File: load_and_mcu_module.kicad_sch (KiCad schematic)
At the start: 1 part, among them M2 LP-MSPM0G3519

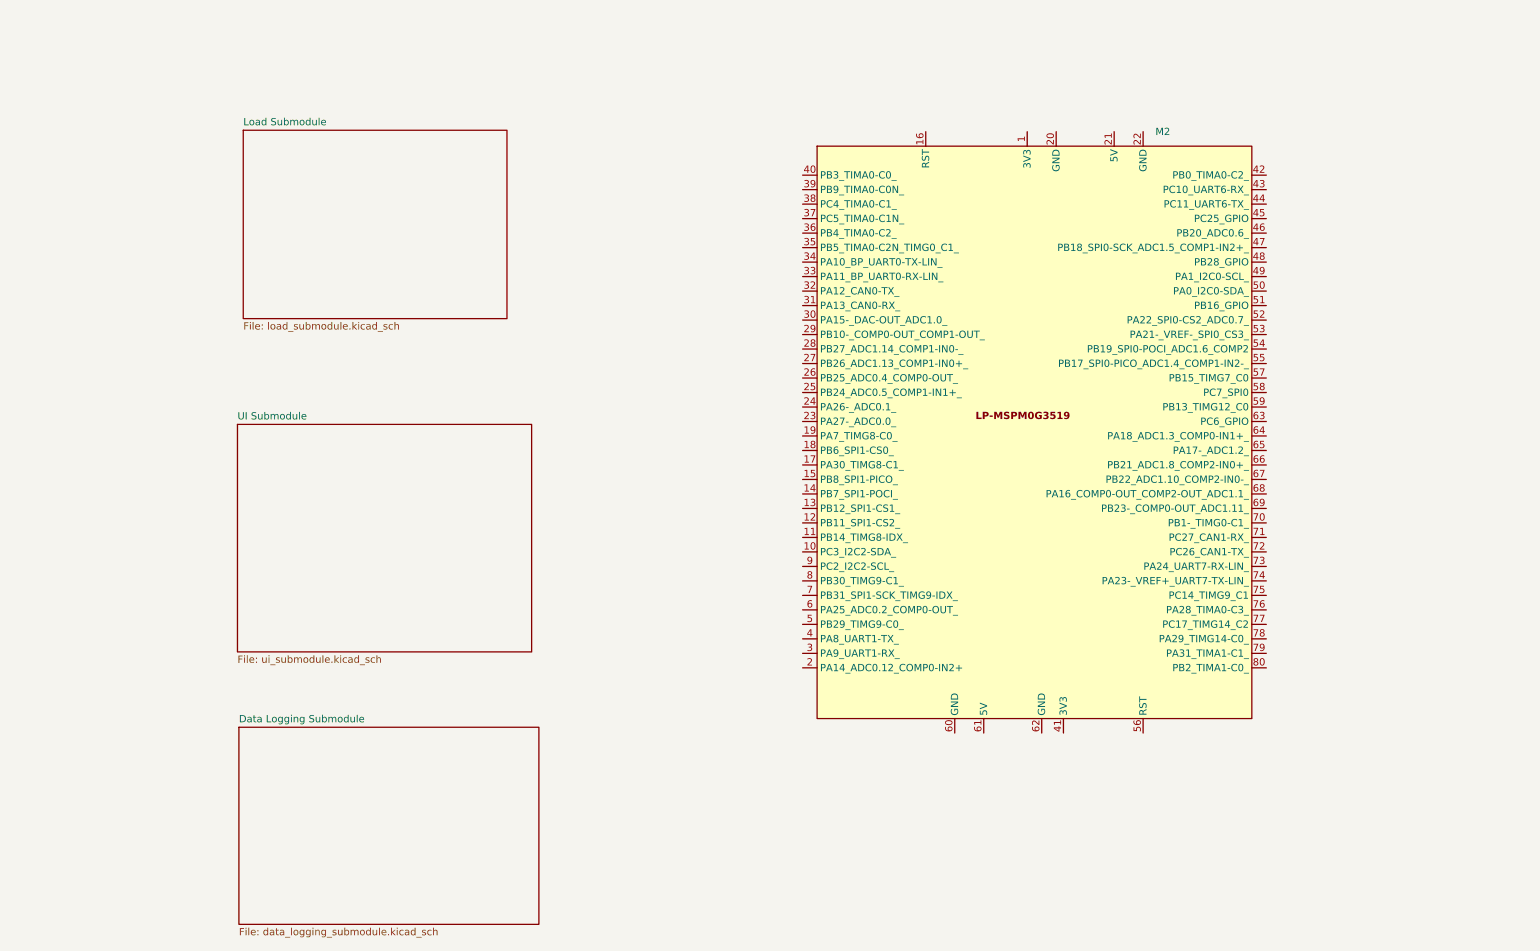
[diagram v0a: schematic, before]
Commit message: Finished Squematics V1
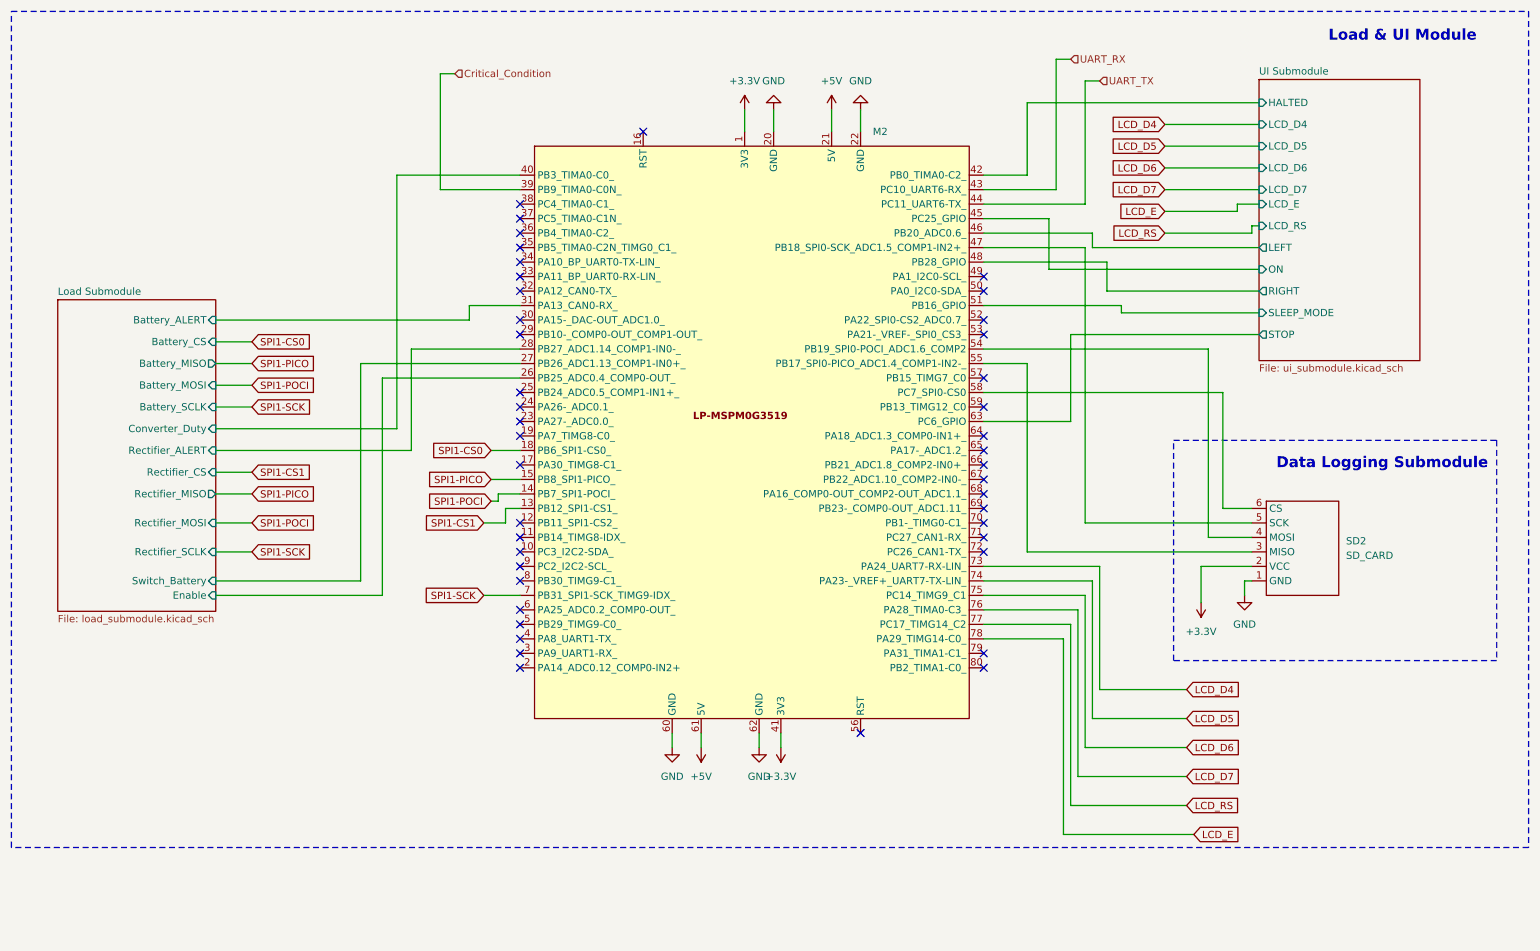
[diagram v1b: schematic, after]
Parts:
- added SD2: SD_CARD, symbol windTurbineSchemSymLib:SD_Card_Adapter
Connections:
- net +3.3V: now reaches M2.1 (3V3)
- net +3.3V: now also M2.41 (3V3), SD2.2 (VCC)
- net SPI1-CS1: now reaches M2.13 (PB12_SPI1-CS1_)
- net SPI1-POCI: now reaches M2.14 (PB7_SPI1-POCI_)
- net SPI1-PICO: now reaches M2.15 (PB8_SPI1-PICO_)
- net SPI1-CS0: now reaches M2.18 (PB6_SPI1-CS0_)
- net GND: now reaches M2.20 (GND)
- net GND: now also M2.22 (GND), M2.60 (GND), M2.62 (GND), SD2.1 (GND)
- net +5V: now reaches M2.21 (5V)
- net +5V: now also M2.61 (5V)
- net Load Submodule/Enable: now reaches M2.26 (PB25_ADC0.4_COMP0-OUT_)
- net Load Submodule/Switch_Battery: now reaches M2.27 (PB26_ADC1.13_COMP1-IN0+_)
- net Load Submodule/Rectifier_ALERT: now reaches M2.28 (PB27_ADC1.14_COMP1-IN0-_)
- net Load Submodule/Battery_ALERT: now reaches M2.31 (PA13_CAN0-RX_)
- net Critical_Condition: now reaches M2.39 (PB9_TIMA0-C0N_)
- net Load Submodule/Converter_Duty: now reaches M2.40 (PB3_TIMA0-C0_)
- net UI Submodule/HALTED: now reaches M2.42 (PB0_TIMA0-C2_)
- net UART_RX: now reaches M2.43 (PC10_UART6-RX_)
- net UART_TX: now reaches M2.44 (PC11_UART6-TX_)
- net UI Submodule/ON: now reaches M2.45 (PC25_GPIO)
- net UI Submodule/LEFT: now reaches M2.46 (PB20_ADC0.6_)
- net at M2.47 (PB18_SPI0-SCK_ADC1.5_COMP1-IN2+_): now also SD2.5 (SCK)
- net UI Submodule/RIGHT: now reaches M2.48 (PB28_GPIO)
- net UI Submodule/SLEEP_MODE: now reaches M2.51 (PB16_GPIO)
- net at M2.54 (PB19_SPI0-POCI_ADC1.6_COMP2): now also SD2.4 (MOSI)
- net at M2.55 (PB17_SPI0-PICO_ADC1.4_COMP1-IN2-_): now also SD2.3 (MISO)
- net at M2.58 (PC7_SPI0-CS0): now also SD2.6 (CS)
- net UI Submodule/STOP: now reaches M2.63 (PC6_GPIO)
- net SPI1-SCK: now reaches M2.7 (PB31_SPI1-SCK_TIMG9-IDX_)
- net LCD_D4: now reaches M2.73 (PA24_UART7-RX-LIN_)
- net LCD_D5: now reaches M2.74 (PA23-_VREF+_UART7-TX-LIN_)
- net LCD_D6: now reaches M2.75 (PC14_TIMG9_C1)
- net LCD_D7: now reaches M2.76 (PA28_TIMA0-C3_)
- net LCD_RS: now reaches M2.77 (PC17_TIMG14_C2)
- net LCD_E: now reaches M2.78 (PA29_TIMG14-C0_)
- no-connect marks 0 -> 43
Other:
- removed sheet Data Logging Submodule
- sheet Load Submodule ports: added Battery_ALERT, Battery_CS, Battery_MISO, Battery_MOSI, Battery_SCLK, Converter_Duty, Enable, Rectifier_ALERT, Rectifier_CS, Rectifier_MISO, Rectifier_MOSI, Rectifier_SCLK, Switch_Battery; removed none
- sheet UI Submodule ports: added HALTED, LCD_D4, LCD_D5, LCD_D6, LCD_D7, LCD_E, LCD_RS, LEFT, ON, RIGHT, SLEEP_MODE, STOP; removed none
- note added: "Data Logging Submodule"
- note added: "Load & UI Module"
- company: (none) -> PRES
- title: (none) -> Load & UI Module
- moved on the sheet: M2

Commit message: Added better colors
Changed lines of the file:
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@@
 		)
 		(fill
-			(color 0 0 0 0.0000)
+			(color 255 255 194 1.0000)
 		)
 		(property "Sheetname" "UI Submodule"
@@
 		)
 		(fill
-			(color 0 0 0 0.0000)
+			(color 255 255 194 1.0000)
 		)
 		(property "Sheetname" "Load Submodule"
